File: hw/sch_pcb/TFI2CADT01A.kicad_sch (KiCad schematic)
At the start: 38 parts, among them J1 SM04B-GHS-TB, J2 SM04B-GHS-TB, J3 SM04B-GHS-TB, J4 SM04B-GHS-TB, J5 SM04B-GHS-TB, J6 SM04B-GHS-TB, M1 HOLE, M2 HOLE, M3 HOLE, M4 HOLE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

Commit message: uprava schema, sablona
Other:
- moved on the sheet: J4
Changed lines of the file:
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@@
     (stroke (width 0) (type default) (color 0 0 0 0))
-  )
-  (wire (pts (xy 231.14 75.565) (xy 240.03 75.565))
-    (stroke (width 0) (type solid) (color 0 0 0 0))
   )
   (wire (pts (xy 40.64 165.1) (xy 40.64 166.37))
@@
     (stroke (width 0) (type solid) (color 0 0 0 0))
   )
-  (wire (pts (xy 240.03 80.645) (xy 238.76 80.645))
+  (wire (pts (xy 240.03 80.01) (xy 238.76 80.645))
     (stroke (width 0) (type solid) (color 0 0 0 0))
   )
@@
     (stroke (width 0) (type dash) (color 0 0 0 0))
   )
-  (wire (pts (xy 240.03 78.105) (xy 238.76 78.105))
+  (wire (pts (xy 240.03 77.47) (xy 238.76 78.105))
     (stroke (width 0) (type solid) (color 0 0 0 0))
   )
@@
     (stroke (width 0) (type default) (color 0 0 0 0))
   )
-  (wire (pts (xy 238.76 70.485) (xy 240.03 70.485))
-    (stroke (width 0) (type solid) (color 0 0 0 0))
-  )
-  (wire (pts (xy 238.76 80.645) (xy 238.76 83.185))
+  (wire (pts (xy 238.76 69.85) (xy 240.03 69.85))
+    (stroke (width 0) (type solid) (color 0 0 0 0))
+  )
+  (wire (pts (xy 238.76 80.645) (xy 238.76 82.55))
     (stroke (width 0) (type solid) (color 0 0 0 0))
   )
@@
   (wire (pts (xy 163.195 146.685) (xy 163.195 156.21))
     (stroke (width 0) (type default) (color 0 0 0 0))
-  )
-  (wire (pts (xy 231.14 73.025) (xy 240.03 73.025))
-    (stroke (width 0) (type solid) (color 0 0 0 0))
   )
   (wire (pts (xy 55.88 167.64) (xy 55.88 166.37))
@@
     (effects (font (size 1.524 1.524)) (justify left bottom))
   )
-  (label "SDAout1" (at 231.14 75.565 0) (fields_autoplaced)
-    (effects (font (size 1.524 1.524)) (justify left bottom))
+  (label "SDAout1" (at 240.03 74.93 180) (fields_autoplaced)
+    (effects (font (size 1.524 1.524)) (justify right bottom))
   )
   (label "SCLout1" (at 193.04 73.025 0) (fields_autoplaced)
@@
     (effects (font (size 1.524 1.524)) (justify right bottom))
   )
-  (label "SCLout1" (at 231.14 73.025 0) (fields_autoplaced)
-    (effects (font (size 1.524 1.524)) (justify left bottom))
+  (label "SCLout1" (at 240.03 72.39 180) (fields_autoplaced)
+    (effects (font (size 1.524 1.524)) (justify right bottom))
   )
   (label "SDAin" (at 77.47 83.185 180) (fields_autoplaced)
@@
     )
   )
-  (symbol (lib_id "power:GND") (at 238.76 83.185 0) (unit 1)
-    (in_bom yes) (on_board yes)
-    (property "Reference" "#PWR026" (id 0) (at 238.76 89.535 0)
-      (effects (font (size 1.27 1.27)) hide)
-    )
-    (property "Value" "GND" (id 1) (at 238.887 87.5792 0))
-    (property "Footprint" "" (id 2) (at 238.76 83.185 0)
-      (effects (font (size 1.27 1.27)) hide)
-    )
-    (property "Datasheet" "" (id 3) (at 238.76 83.185 0)
+  (symbol (lib_id "power:GND") (at 238.76 82.55 0) (unit 1)
+    (in_bom yes) (on_board yes)
+    (property "Reference" "#PWR026" (id 0) (at 238.76 88.9 0)
+      (effects (font (size 1.27 1.27)) hide)
+    )
+    (property "Value" "GND" (id 1) (at 238.887 86.9442 0))
+    (property "Footprint" "" (id 2) (at 238.76 82.55 0)
+      (effects (font (size 1.27 1.27)) hide)
+    )
+    (property "Datasheet" "" (id 3) (at 238.76 82.55 0)
       (effects (font (size 1.27 1.27)) hide)
     )
@@
     (pin "1")
   )
-  (symbol (lib_id "power:+5V") (at 238.76 70.485 0) (unit 1)
-    (in_bom yes) (on_board yes)
-    (property "Reference" "#PWR025" (id 0) (at 238.76 74.295 0)
-      (effects (font (size 1.27 1.27)) hide)
-    )
-    (property "Value" "+5V" (id 1) (at 239.141 66.0908 0))
-    (property "Footprint" "" (id 2) (at 238.76 70.485 0)
-      (effects (font (size 1.27 1.27)) hide)
-    )
-    (property "Datasheet" "" (id 3) (at 238.76 70.485 0)
-      (effects (font (size 1.27 1.27)) hide)
-    )
-    (pin "1")
-  )
-  (symbol (lib_id "MLAB_CONNECTORS_JST:SM04B-GHS-TB") (at 245.11 75.565 0) (unit 1)
-    (in_bom yes) (on_board yes)
-    (property "Reference" "J4" (id 0) (at 247.0912 74.0664 0)
+  (symbol (lib_id "power:+5V") (at 238.76 69.85 0) (unit 1)
+    (in_bom yes) (on_board yes)
+    (property "Reference" "#PWR025" (id 0) (at 238.76 73.66 0)
+      (effects (font (size 1.27 1.27)) hide)
+    )
+    (property "Value" "+5V" (id 1) (at 239.141 65.4558 0))
+    (property "Footprint" "" (id 2) (at 238.76 69.85 0)
+      (effects (font (size 1.27 1.27)) hide)
+    )
+    (property "Datasheet" "" (id 3) (at 238.76 69.85 0)
+      (effects (font (size 1.27 1.27)) hide)
+    )
+    (pin "1")
+  )
+  (symbol (lib_id "MLAB_CONNECTORS_JST:SM04B-GHS-TB") (at 245.11 74.93 0) (unit 1)
+    (in_bom yes) (on_board yes)
+    (property "Reference" "J4" (id 0) (at 247.0912 73.4314 0)
       (effects (font (size 1.524 1.524)) (justify left))
     )
-    (property "Value" "SM04B-GHS-TB" (id 1) (at 247.0912 76.7842 0)
+    (property "Value" "SM04B-GHS-TB" (id 1) (at 247.0912 76.1492 0)
       (effects (font (size 1.524 1.524)) (justify left))
     )
-    (property "Footprint" "Connector_JST:JST_GH_SM04B-GHS-TB_1x04-1MP_P1.25mm_Horizontal" (id 2) (at 245.11 70.485 0)
+    (property "Footprint" "Connector_JST:JST_GH_SM04B-GHS-TB_1x04-1MP_P1.25mm_Horizontal" (id 2) (at 245.11 69.85 0)
       (effects (font (size 1.524 1.524)) hide)
     )
-    (property "Datasheet" "" (id 3) (at 245.11 70.485 0)
-      (effects (font (size 1.524 1.524)))
-    )
-    (property "UST_id" "" (id 4) (at 245.11 75.565 0)
-      (effects (font (size 1.27 1.27)) hide)
-    )
-    (property "UST_ID" "5c86273d1287500b4e0280be" (id 5) (at 245.11 75.565 0)
-      (effects (font (size 1.27 1.27)) hide)
-    )
+    (property "Datasheet" "" (id 3) (at 245.11 69.85 0)
+      (effects (font (size 1.524 1.524)))
+    )
+    (property "UST_id" "" (id 4) (at 245.11 74.93 0)
+      (effects (font (size 1.27 1.27)) hide)
+    )
+    (property "UST_ID" "5c86273d1287500b4e0280be" (id 5) (at 245.11 74.93 0)
+      (effects (font (size 1.27 1.27)) hide)
+    )

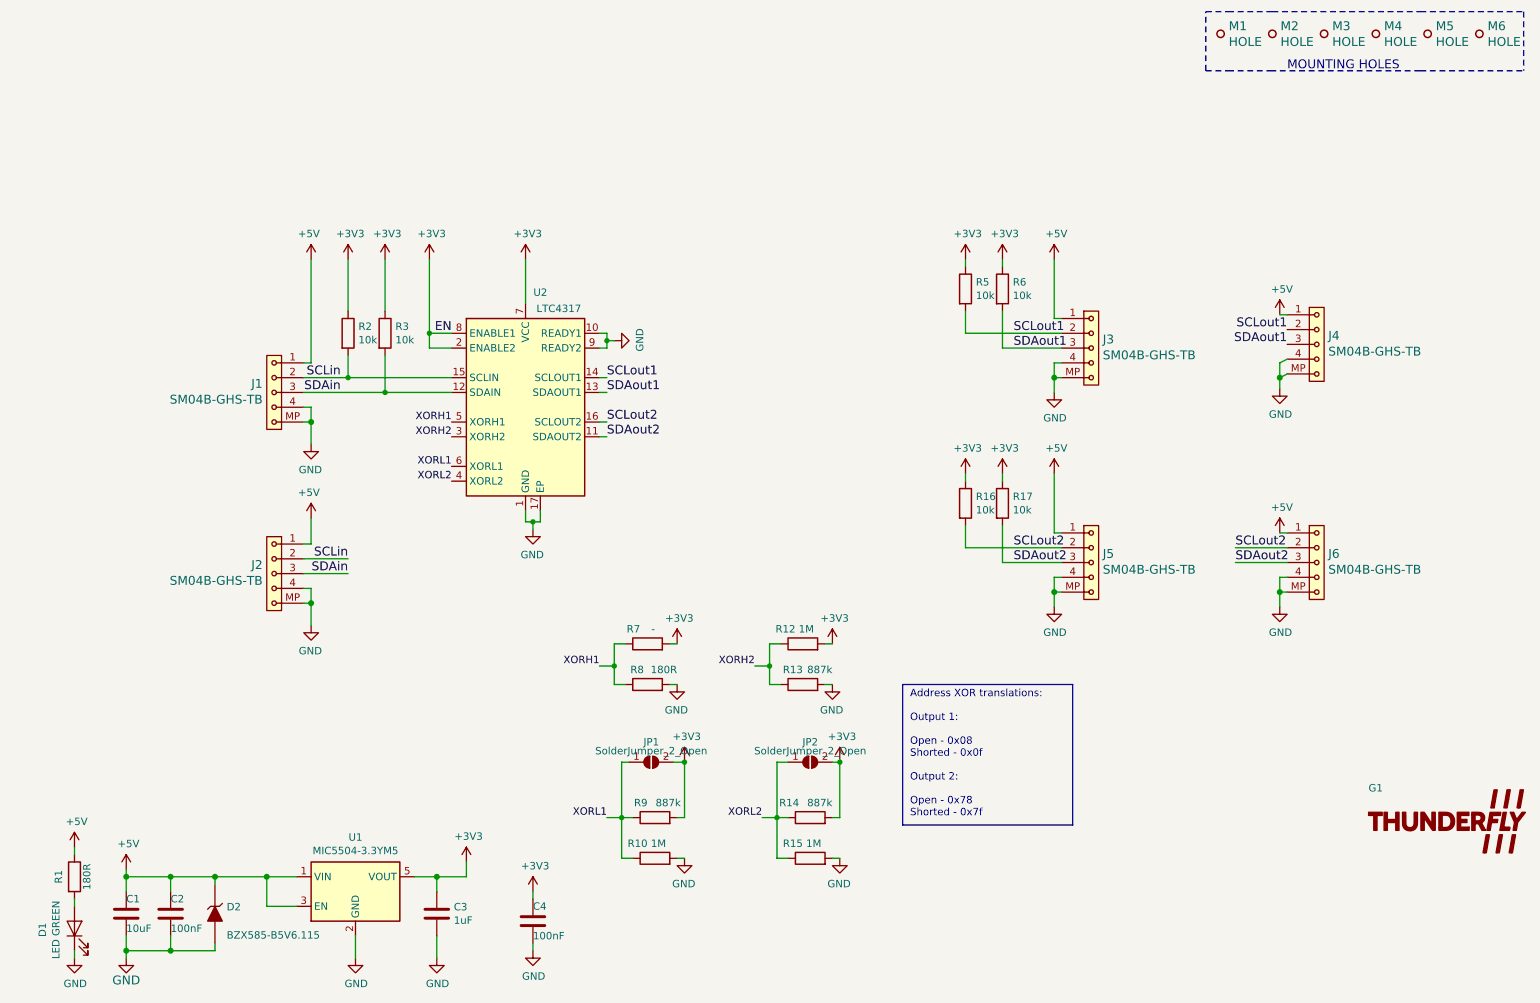
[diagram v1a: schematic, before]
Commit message: Update Titleblock Move PCB to center of the page Move grid origin to the bottom left corner of the PCB
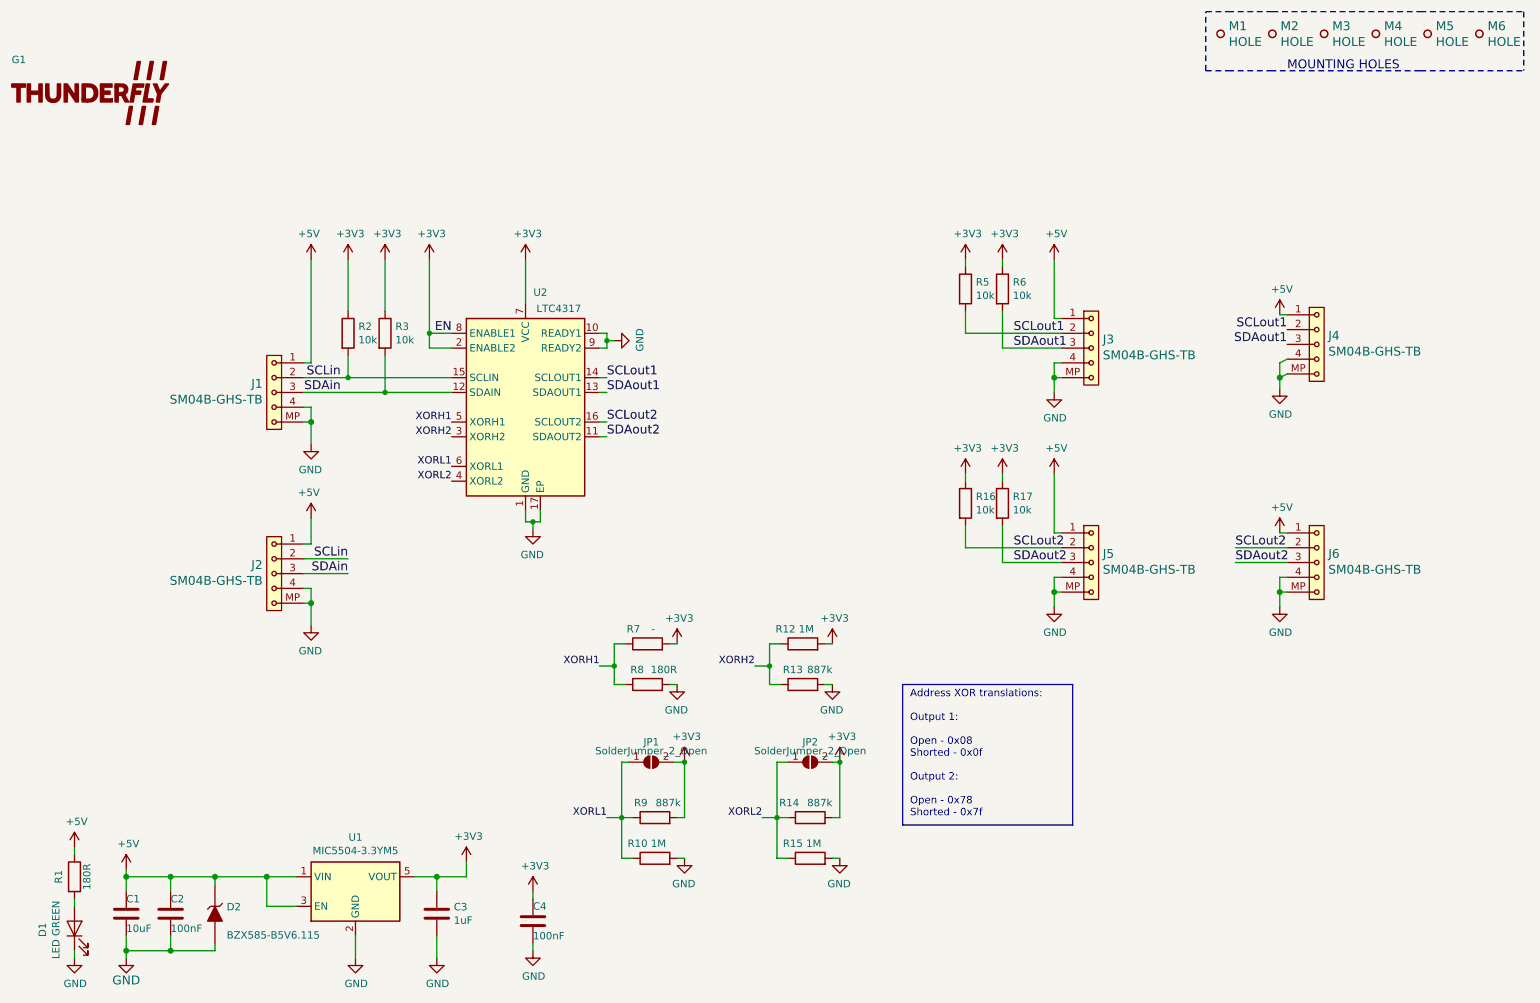
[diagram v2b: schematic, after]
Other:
- moved on the sheet: G1
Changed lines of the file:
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@@
     (date "2021-04-05")
     (company "ThunderFly s.r.o.")
-    (comment 1 "I2C expander")
+    (comment 1 "I2C address translator")
     (comment 2 "Jacho  <info@thunderfly.cz>")
   )
@@
     (pin "2")
   )
-  (symbol (lib_id "MLAB_TF_LOGO:LOGO") (at 267.335 156.845 0) (unit 1)
+  (symbol (lib_id "MLAB_TF_LOGO:LOGO") (at 34.29 31.75 0) (unit 1)
     (in_bom no) (on_board yes)
-    (property "Reference" "G1" (id 0) (at 254 151.13 0)
-      (effects (font (size 1.27 1.27)) (justify left))
-    )
-    (property "Value" "LOGO" (id 1) (at 267.335 163.3126 0)
-      (effects (font (size 1.27 1.27)) hide)
-    )
-    (property "Footprint" "MLAB_LOGA:TF 10x4,7" (id 2) (at 267.335 156.845 0)
-      (effects (font (size 1.27 1.27)) hide)
-    )
-    (property "Datasheet" "" (id 3) (at 267.335 156.845 0)
-      (effects (font (size 1.27 1.27)) hide)
-    )
+    (property "Reference" "G1" (id 0) (at 20.955 26.035 0)
+      (effects (font (size 1.27 1.27)) (justify left))
+    )
+    (property "Value" "LOGO" (id 1) (at 34.29 38.2176 0)
+      (effects (font (size 1.27 1.27)) hide)
+    )
+    (property "Footprint" "MLAB_LOGA:TF 10x4,7" (id 2) (at 34.29 31.75 0)
+      (effects (font (size 1.27 1.27)) hide)
+    )
+    (property "Datasheet" "" (id 3) (at 34.29 31.75 0)
+      (effects (font (size 1.27 1.27)) hide)
+    )

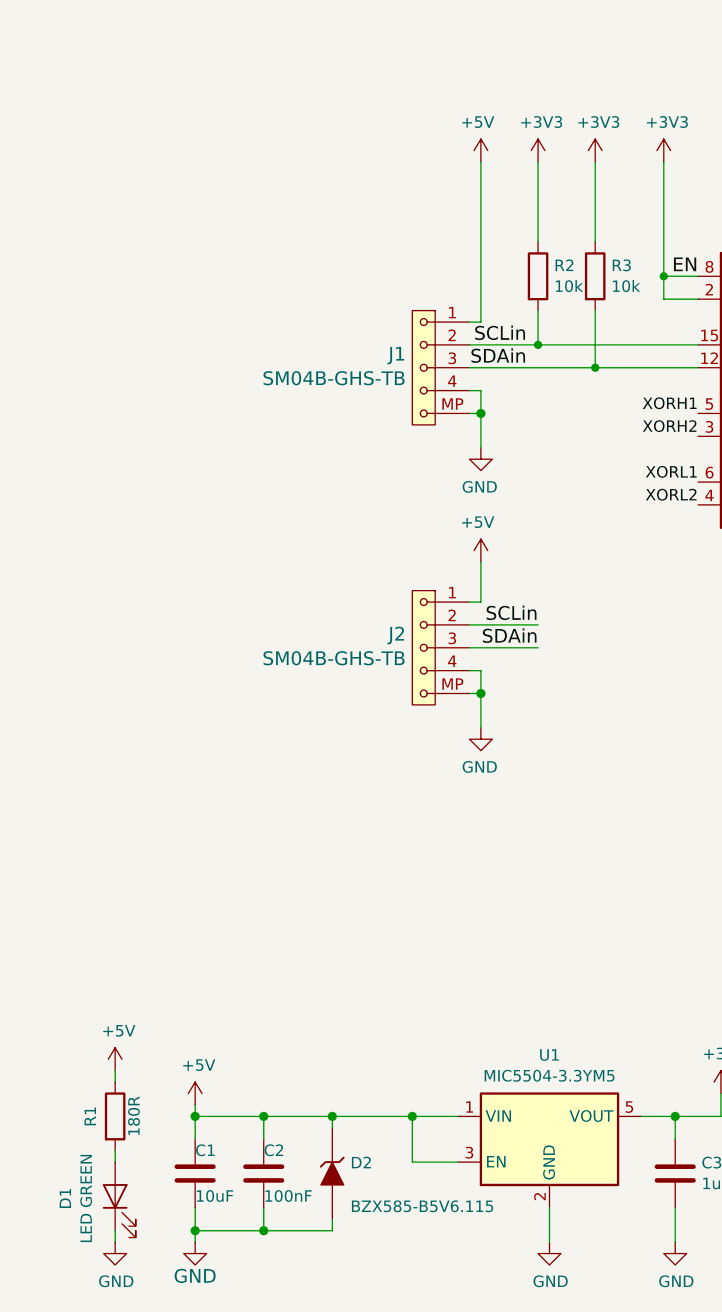
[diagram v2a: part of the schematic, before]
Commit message: Resolve ERC issues by adding power flags and updating symbols. Update PCB from schematics.
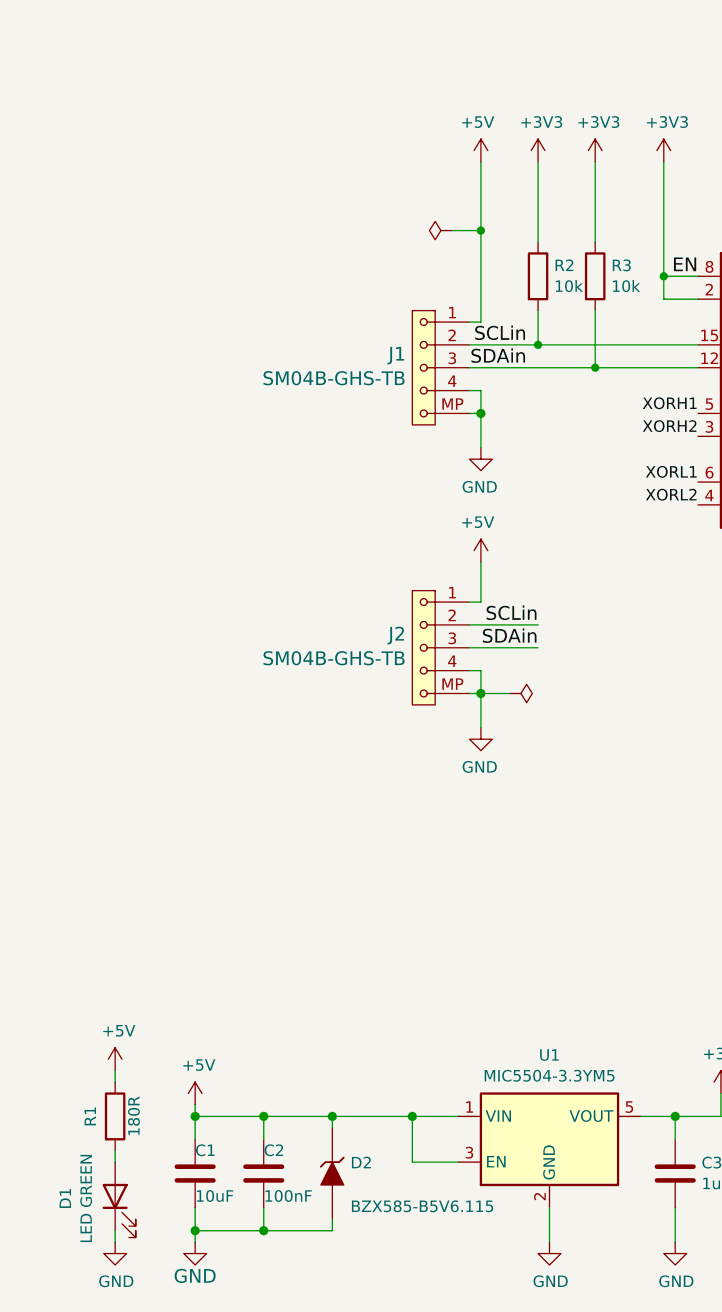
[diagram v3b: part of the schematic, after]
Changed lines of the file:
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@@
   (junction (at 124.46 130.175) (diameter 0) (color 0 0 0 0)
+  )
+  (junction (at 72.39 67.945) (diameter 0) (color 0 0 0 0)
   )
   (junction (at 40.64 179.07) (diameter 1.016) (color 0 0 0 0)
@@
     (stroke (width 0) (type solid) (color 0 0 0 0))
   )
-  (wire (pts (xy 72.39 60.325) (xy 72.39 78.105))
+  (wire (pts (xy 72.39 60.325) (xy 72.39 67.945))
     (stroke (width 0) (type default) (color 0 0 0 0))
   )
@@
     (stroke (width 0) (type default) (color 0 0 0 0))
   )
+  (wire (pts (xy 72.39 67.945) (xy 72.39 78.105))
+    (stroke (width 0) (type default) (color 0 0 0 0))
+  )
   (wire (pts (xy 127.635 163.195) (xy 125.73 163.195))
     (stroke (width 0) (type default) (color 0 0 0 0))
@@
     (stroke (width 0) (type default) (color 0 0 0 0))
   )
+  (wire (pts (xy 69.215 67.945) (xy 72.39 67.945))
+    (stroke (width 0) (type default) (color 0 0 0 0))
+  )
   (wire (pts (xy 93.98 166.37) (xy 93.98 168.91))
     (stroke (width 0) (type solid) (color 0 0 0 0))
@@
   )
   (wire (pts (xy 191.135 75.565) (xy 201.295 75.565))
+    (stroke (width 0) (type default) (color 0 0 0 0))
+  )
+  (wire (pts (xy 72.39 119.38) (xy 75.565 119.38))
     (stroke (width 0) (type default) (color 0 0 0 0))
   )
@@
     (pin "1")
     (pin "2")
+  )
+  (symbol (lib_id "power:PWR_FLAG") (at 75.565 119.38 270) (unit 1)
+    (in_bom yes) (on_board yes) (fields_autoplaced)
+    (property "Reference" "#FLG0102" (id 0) (at 77.47 119.38 0)
+      (effects (font (size 1.27 1.27)) hide)
+    )
+    (property "Value" "" (id 1) (at 78.74 119.8138 90)
+      (effects (font (size 1.27 1.27)) (justify left))
+    )
+    (property "Footprint" "" (id 2) (at 75.565 119.38 0)
+      (effects (font (size 1.27 1.27)) hide)
+    )
+    (property "Datasheet" "~" (id 3) (at 75.565 119.38 0)
+      (effects (font (size 1.27 1.27)) hide)
+    )
+    (pin "1")
   )
   (symbol (lib_id "MLAB_TF_LOGO:LOGO") (at 34.29 31.75 0) (unit 1)
@@
     (pin "2")
   )
-  (symbol (lib_name "HOLE_TF_5") (lib_id "MLAB_MECHANICAL:HOLE_TF") (at 273.05 21.59 90) (unit 1)
+  (symbol (lib_id "MLAB_MECHANICAL:HOLE_TF") (at 273.05 21.59 90) (unit 1)
     (in_bom yes) (on_board yes) (fields_autoplaced)
     (property "Reference" "M6" (id 0) (at 274.4471 20.2579 90)
@@
     (pin "1")
   )
-  (symbol (lib_name "HOLE_TF_2") (lib_id "MLAB_MECHANICAL:HOLE_TF") (at 255.27 21.59 90) (unit 1)
+  (symbol (lib_id "MLAB_MECHANICAL:HOLE_TF") (at 255.27 21.59 90) (unit 1)
     (in_bom yes) (on_board yes) (fields_autoplaced)
     (property "Reference" "M4" (id 0) (at 256.6671 20.2579 90)
@@
     (pin "1")
   )
-  (symbol (lib_name "HOLE_TF_3") (lib_id "MLAB_MECHANICAL:HOLE_TF") (at 246.38 21.59 90) (unit 1)
+  (symbol (lib_id "MLAB_MECHANICAL:HOLE_TF") (at 246.38 21.59 90) (unit 1)
     (in_bom yes) (on_board yes)
     (property "Reference" "M3" (id 0) (at 247.7771 20.2579 90)
@@
     (pin "1")
     (pin "2")
+  )
+  (symbol (lib_id "power:PWR_FLAG") (at 69.215 67.945 90) (unit 1)
+    (in_bom yes) (on_board yes) (fields_autoplaced)
+    (property "Reference" "#FLG0101" (id 0) (at 67.31 67.945 0)
+      (effects (font (size 1.27 1.27)) hide)
+    )
+    (property "Value" "" (id 1) (at 66.0401 68.3788 90)
+      (effects (font (size 1.27 1.27)) (justify left))
+    )
+    (property "Footprint" "" (id 2) (at 69.215 67.945 0)
+      (effects (font (size 1.27 1.27)) hide)
+    )
+    (property "Datasheet" "~" (id 3) (at 69.215 67.945 0)
+      (effects (font (size 1.27 1.27)) hide)
+    )
+    (pin "1")
   )
   (symbol (lib_id "Device:R") (at 130.175 133.35 90) (unit 1)
@@
     (pin "1")
   )
-  (symbol (lib_name "HOLE_TF_4") (lib_id "MLAB_MECHANICAL:HOLE_TF") (at 237.49 21.59 90) (unit 1)
+  (symbol (lib_id "MLAB_MECHANICAL:HOLE_TF") (at 237.49 21.59 90) (unit 1)
     (in_bom yes) (on_board yes) (fields_autoplaced)
     (property "Reference" "M2" (id 0) (at 238.8871 20.2579 90)
@@
     (pin "2")
   )
-  (symbol (lib_name "HOLE_TF_1") (lib_id "MLAB_MECHANICAL:HOLE_TF") (at 228.6 21.59 90) (unit 1)
+  (symbol (lib_id "MLAB_MECHANICAL:HOLE_TF") (at 228.6 21.59 90) (unit 1)
     (in_bom yes) (on_board yes) (fields_autoplaced)
     (property "Reference" "M1" (id 0) (at 229.9971 20.2579 90)
@@
   )
   (symbol_instances
+    (path "/46b2da9b-f25f-40d0-bae8-be60a1cafa29"
+      (reference "#FLG0101") (unit 1) (value "PWR_FLAG") (footprint "")
+    )
+    (path "/036b2aca-36bb-4ef0-a72a-fa41b69ff1ef"
+      (reference "#FLG0102") (unit 1) (value "PWR_FLAG") (footprint "")
+    )
     (path "/214f72e0-6ab3-470d-ba9e-d69be96682bc"
       (reference "#PWR01") (unit 1) (value "+5V") (footprint "")
